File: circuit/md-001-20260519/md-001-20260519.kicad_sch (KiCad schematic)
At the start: 11 parts, among them J1 VIN-motor

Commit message: Update MD基板を更新
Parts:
- added C10, C6, C9: 22n, symbol Device:C_Small
- added C11, C12, C8: 220n, symbol Device:C_Small
- added C4: 100n, symbol Device:C_Small
- added R10, R2, R9: 2.49k, symbol Device:R_Small
- added R11, R13, R5: 10k, symbol Device:R_Small
- added R12, R14, R6: NP, symbol Device:R_Small
- added R15, R16, R8: 20k, symbol Device:R_Small
- added U2, U3, U4: (no value), symbol @Thrive_symbol_md:DRV8874
- renumbered C3 to C1, C4 to C2, C5 to C3, C1 to C5, C2 to C7, R2 to R3, R3 to R4, R4 to R7
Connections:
- net +3.3V: now also C4.1, R11.1, R13.1, R5.1, U2.3 (SLEEP), U3.3 (SLEEP), U4.3 (SLEEP)
- net GND: now also C4.2, R10.2, R12.2, R14.2, R15.2, R16.2, R2.2, R6.2, R8.2, R9.2, U2.15 (GND), U2.16 (PMODE), U2.17 (GND), U2.9 (PGND), U3.15 (GND), U3.16 (PMODE), U3.17 (GND), U3.9 (PGND), U4.15 (GND), U4.16 (PMODE), U4.17 (GND), U4.9 (PGND)
- net VCC: now also C11.2, C12.2, C8.2, U2.11 (VM), U3.11 (VM), U4.11 (VM)
- new net: C12.1, U4.12 (VCP)
- new net: C10.2, U4.13 (CPH)
- new net: C10.1, U4.14 (CPL)
- new net: R10.1, U4.6 (IPROPI)
- new net: C11.1, U3.12 (VCP)
- new net: C9.2, U3.13 (CPH)
- new net: C9.1, U3.14 (CPL)
- new net: R9.1, U3.6 (IPROPI)
- new net: C8.1, U2.12 (VCP)
- new net: C6.2, U2.13 (CPH)
- new net: C6.1, U2.14 (CPL)
- new net: R2.1, U2.6 (IPROPI)
- new net EN-2: U3.1 (EN)
- new net EN-3: U2.1 (EN)
- new net EN-4: U4.1 (EN)
- new net IMODE-2: R15.1, U3.7 (IMODE)
- new net IMODE-3: R8.1, U2.7 (IMODE)
- new net IMODE-4: R16.1, U4.7 (IMODE)
- new net OUT1-2: U3.8 (OUT1)
- new net OUT1-3: U2.8 (OUT1)
- new net OUT1-4: U4.8 (OUT1)
- new net OUT2-2: U3.10 (OUT2)
- new net OUT2-3: U2.10 (OUT2)
- new net OUT2-4: U4.10 (OUT2)
- new net PH-2: U3.2 (PH)
- new net PH-3: U2.2 (PH)
- new net PH-4: U4.2 (PH)
- new net VREF-2: R11.2, R12.1, U3.5 (VREF)
- new net VREF-3: R5.2, R6.1, U2.5 (VREF)
- new net VREF-4: R13.2, R14.1, U4.5 (VREF)
- no-connect marks 1 -> 4
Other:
- moved on the sheet: C1, C2, C3, C5, C7, J1, R1, R3, R4, R7, U1

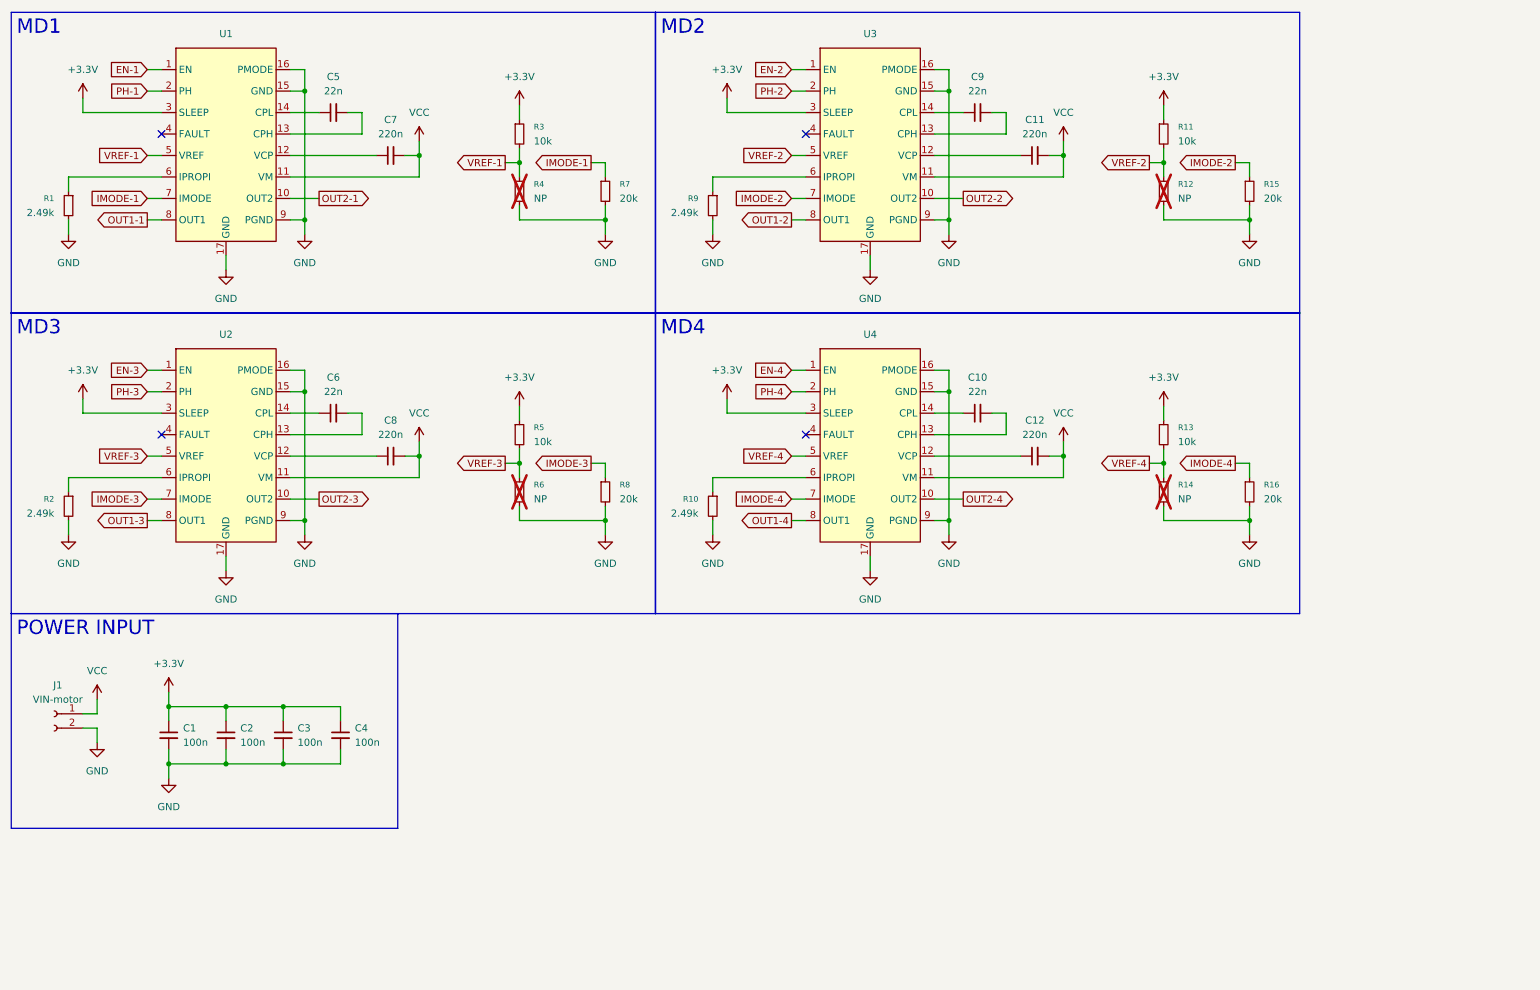
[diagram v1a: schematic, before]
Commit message: Update MD基板の回路図を完成させた
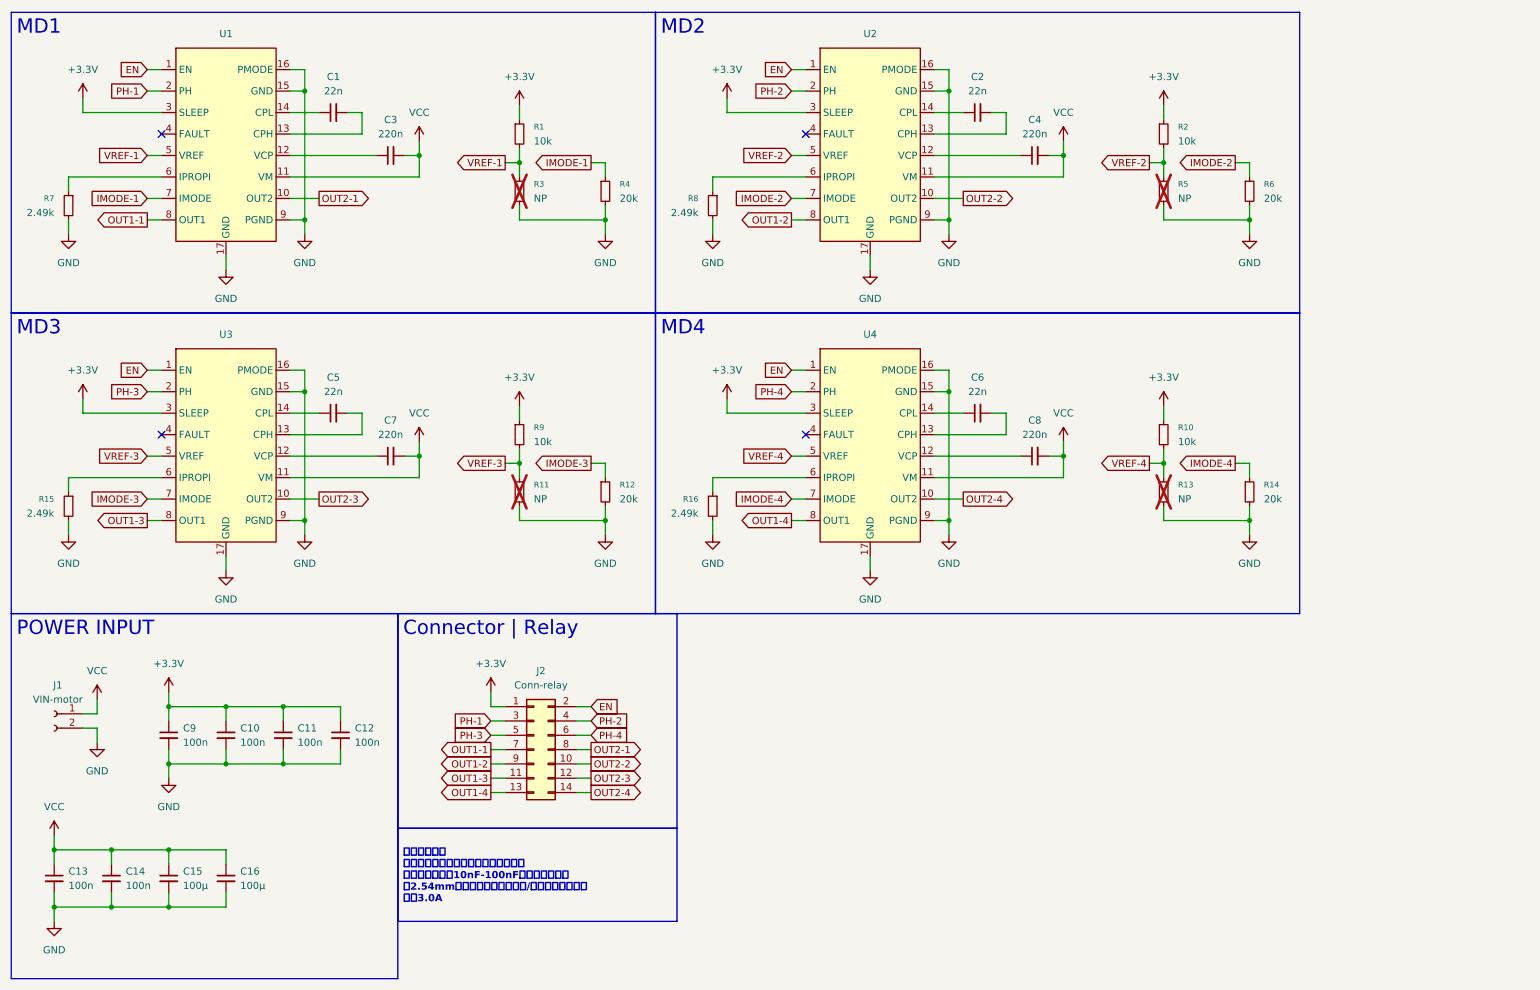
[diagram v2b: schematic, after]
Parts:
- added C13, C14: 100n, Resistor_SMD:R_0603_1608Metric, symbol Device:C_Small
- added C15, C16: 100μ, Resistor_SMD:R_1206_3216Metric, symbol Device:C_Small
- added J2: Conn-relay, Connector_PinSocket_2.54mm:PinSocket_2x07_P2.54mm_Horizontal, symbol Connector_Generic:Conn_02x07_Odd_Even
- C1: renamed from C5; footprint (none) -> Resistor_SMD:R_0603_1608Metric
- C10: renamed from C2; footprint (none) -> Resistor_SMD:R_0603_1608Metric
- C11: renamed from C3; footprint (none) -> Resistor_SMD:R_0603_1608Metric
- C12: renamed from C4; footprint (none) -> Resistor_SMD:R_0603_1608Metric
- C2: renamed from C9; footprint (none) -> Resistor_SMD:R_0603_1608Metric
- C3: renamed from C7; footprint (none) -> Resistor_SMD:R_0603_1608Metric
- C4: renamed from C11; footprint (none) -> Resistor_SMD:R_0603_1608Metric
- C5: renamed from C6; footprint (none) -> Resistor_SMD:R_0603_1608Metric
- C6: renamed from C10; footprint (none) -> Resistor_SMD:R_0603_1608Metric
- C7: renamed from C8; footprint (none) -> Resistor_SMD:R_0603_1608Metric
- C8: renamed from C12; footprint (none) -> Resistor_SMD:R_0603_1608Metric
- C9: renamed from C1; footprint (none) -> Resistor_SMD:R_0603_1608Metric
- J1: footprint (none) -> Connector_AMASS:AMASS_XT30PW-F_1x02_P2.50mm_Horizontal
- R1: renamed from R3; footprint (none) -> Resistor_SMD:R_0603_1608Metric
- R10: renamed from R13; footprint (none) -> Resistor_SMD:R_0603_1608Metric
- R11: renamed from R6; footprint (none) -> Resistor_SMD:R_0603_1608Metric
- R12: renamed from R8; footprint (none) -> Resistor_SMD:R_0603_1608Metric
- R13: renamed from R14; footprint (none) -> Resistor_SMD:R_0603_1608Metric
- R14: renamed from R16; footprint (none) -> Resistor_SMD:R_0603_1608Metric
- R15: renamed from R2; footprint (none) -> Resistor_SMD:R_0603_1608Metric
- R16: renamed from R10; footprint (none) -> Resistor_SMD:R_0603_1608Metric
- R2: renamed from R11; footprint (none) -> Resistor_SMD:R_0603_1608Metric
- R3: renamed from R4; footprint (none) -> Resistor_SMD:R_0603_1608Metric
- R4: renamed from R7; footprint (none) -> Resistor_SMD:R_0603_1608Metric
- R5: renamed from R12; footprint (none) -> Resistor_SMD:R_0603_1608Metric
- R6: renamed from R15; footprint (none) -> Resistor_SMD:R_0603_1608Metric
- R7: renamed from R1; footprint (none) -> Resistor_SMD:R_0603_1608Metric
- R8: renamed from R9; footprint (none) -> Resistor_SMD:R_0603_1608Metric
- R9: renamed from R5; footprint (none) -> Resistor_SMD:R_0603_1608Metric
- U1, U4: footprint (none) -> Package_SO:HTSSOP-16-1EP_4.4x5mm_P0.65mm_EP3.4x5mm_Mask2.66x2.46mm
- U2: renamed from U3; footprint (none) -> Package_SO:HTSSOP-16-1EP_4.4x5mm_P0.65mm_EP3.4x5mm_Mask2.66x2.46mm
- U3: renamed from U2; footprint (none) -> Package_SO:HTSSOP-16-1EP_4.4x5mm_P0.65mm_EP3.4x5mm_Mask2.66x2.46mm
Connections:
- net EN-2 is gone; now on net EN: U2.1 (EN)
- net EN-3 is gone; now on net EN: U3.1 (EN)
- net EN-4 is gone; now on net EN: U4.1 (EN)
- net +3.3V: now also J2.1 (Pin_1)
- net GND: now also C13.2, C14.2, C15.2, C16.2
- net OUT1-1: now also J2.7 (Pin_7)
- net OUT1-2: now also J2.9 (Pin_9)
- net OUT1-3: now also J2.11 (Pin_11)
- net OUT1-4: now also J2.13 (Pin_13)
- net OUT2-1: now also J2.8 (Pin_8)
- net OUT2-2: now also J2.10 (Pin_10)
- net OUT2-3: now also J2.12 (Pin_12)
- net OUT2-4: now also J2.14 (Pin_14)
- net PH-1: now also J2.3 (Pin_3)
- net PH-2: now also J2.4 (Pin_4)
- net PH-3: now also J2.5 (Pin_5)
- net PH-4: now also J2.6 (Pin_6)
- net VCC: now also C13.1, C14.1, C15.1, C16.1
- net EN-1 renamed EN
- net EN: now also J2.2 (Pin_2)

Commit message: Update いったんMD完成
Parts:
- removed C14: 100n, Resistor_SMD:R_0603_1608Metric, symbol Device:C_Small
- removed C16: 100μ, Resistor_SMD:R_1206_3216Metric, symbol Device:C_Small
- renumbered C15 to C14
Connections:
- net +3.3V: now also J2.4 (Pin_4); no longer J2.1 (Pin_1)
- net EN: now also J2.6 (Pin_6); no longer J2.2 (Pin_2)
- net OUT1-1: now also J2.2 (Pin_2); no longer J2.7 (Pin_7)
- net OUT1-2: now also J2.3 (Pin_3); no longer J2.9 (Pin_9)
- net OUT1-3: now also J2.7 (Pin_7); no longer J2.11 (Pin_11)
- net OUT1-4: now also J2.11 (Pin_11); no longer J2.13 (Pin_13)
- net OUT2-1: now also J2.1 (Pin_1); no longer J2.8 (Pin_8)
- net OUT2-2: now also J2.5 (Pin_5); no longer J2.10 (Pin_10)
- net OUT2-3: now also J2.9 (Pin_9); no longer J2.12 (Pin_12)
- net OUT2-4: now also J2.13 (Pin_13); no longer J2.14 (Pin_14)
- net PH-1: now also J2.8 (Pin_8); no longer J2.3 (Pin_3)
- net PH-2: now also J2.10 (Pin_10); no longer J2.4 (Pin_4)
- net PH-3: now also J2.12 (Pin_12); no longer J2.5 (Pin_5)
- net PH-4: now also J2.14 (Pin_14); no longer J2.6 (Pin_6)
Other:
- moved on the sheet: C14

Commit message: Update DRしてもらったのでMDを修正更新
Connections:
- net GND: now also J1.1 (Pin_1); no longer J1.2 (Pin_2)
- net VCC: now also J1.2 (Pin_2); no longer J1.1 (Pin_1)
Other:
- moved on the sheet: J1
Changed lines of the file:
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@@
 	(symbol
 		(lib_id "Connector:Conn_01x02_Socket")
-		(at 20.32 137.16 0)
-		(mirror y)
+		(at 20.32 139.7 180)
 		(unit 1)
 		(body_style 1)
@@
 		(in_pos_files yes)
 		(dnp no)
-		(fields_autoplaced yes)
 		(property "Reference" "J1"
-			(at 20.955 132.08 0)
+			(at 20.955 144.78 0)
 			(show_name no)
 			(do_not_autoplace no)
@@
 		)
 		(property "Value" "VIN-motor"
-			(at 20.955 134.62 0)
+			(at 20.955 142.24 0)
 			(show_name no)
 			(do_not_autoplace no)
@@
 		)
 		(property "Footprint" "Connector_AMASS:AMASS_XT30PW-F_1x02_P2.50mm_Horizontal"
-			(at 20.32 137.16 0)
+			(at 20.32 139.7 0)
 			(hide yes)
 			(show_name no)
@@
 		)
 		(property "Datasheet" ""
-			(at 20.32 137.16 0)
+			(at 20.32 139.7 0)
 			(hide yes)
 			(show_name no)
@@
 		)
 		(property "Description" "Generic connector, single row, 01x02, script generated"
-			(at 20.32 137.16 0)
+			(at 20.32 139.7 0)
 			(hide yes)
 			(show_name no)

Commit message: Update MD基板を更新
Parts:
- removed J2: Conn-relay, Connector_PinSocket_2.54mm:PinSocket_2x07_P2.54mm_Horizontal, symbol Connector_Generic:Conn_02x07_Odd_Even
- added J2: Conn_Ball_Catch, Connector_PinSocket_2.54mm:PinSocket_1x03_P2.54mm_Vertical, symbol Connector:Conn_01x03_Socket
- added J3: Conn_relay, Connector_PinSocket_2.54mm:PinSocket_2x08_P2.54mm_Horizontal, symbol Connector_Generic:Conn_02x08_Odd_Even
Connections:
- net +3.3V: now also J2.2 (Pin_2), J3.2 (Pin_2)
- net EN: now also J3.6 (Pin_6)
- net GND: now also J2.3 (Pin_3), J3.4 (Pin_4)
- net OUT1-1: now also J3.1 (Pin_1)
- net OUT1-2: now also J3.5 (Pin_5)
- net OUT1-3: now also J3.9 (Pin_9)
- net OUT1-4: now also J3.13 (Pin_13)
- net OUT2-1: now also J3.3 (Pin_3)
- net OUT2-2: now also J3.7 (Pin_7)
- net OUT2-3: now also J3.11 (Pin_11)
- net OUT2-4: now also J3.15 (Pin_15)
- net PH-1: now also J3.8 (Pin_8)
- net PH-2: now also J3.10 (Pin_10)
- net PH-3: now also J3.12 (Pin_12)
- net PH-4: now also J3.14 (Pin_14)
- new net BALL_CATCH: J2.1 (Pin_1), J3.16 (Pin_16)

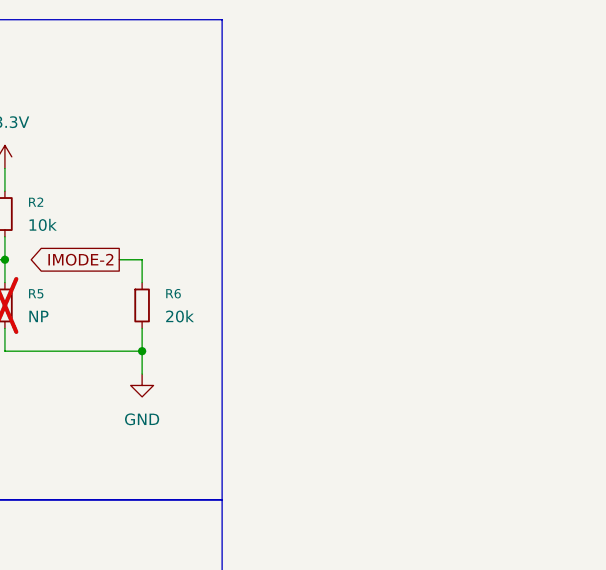
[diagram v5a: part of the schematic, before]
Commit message: Update MD基板のボード図を更新
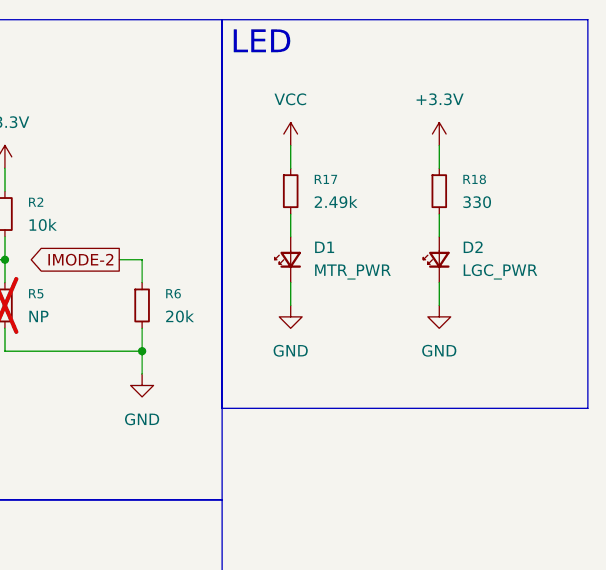
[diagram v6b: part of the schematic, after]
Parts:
- added D1: MTR_PWR, LED_SMD:LED_0603_1608Metric, symbol Device:LED_Small
- added D2: LGC_PWR, LED_SMD:LED_0603_1608Metric, symbol Device:LED_Small
- added R17: 2.49k, Resistor_SMD:R_0603_1608Metric, symbol Device:R_Small
- added R18: 330, Resistor_SMD:R_0603_1608Metric, symbol Device:R_Small
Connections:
- net +3.3V: now also R18.1
- net GND: now also D1.1 (K), D2.1 (K)
- net VCC: now also R17.1
- new net: D1.2 (A), R17.2
- new net: D2.2 (A), R18.2

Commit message: Create 供給基板の回路図完成
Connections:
- net BALL_CATCH renamed BallCatch_{Back}
- net EN renamed Motor_{EN}
- net OUT1-1 renamed Motor_{OUT1-1}
- net OUT1-2 renamed Motor_{OUT2-1}
- net OUT1-3 renamed Motor_{OUT3-1}
- net OUT1-4 renamed Motor_{OUT4-1}
- net OUT2-1 renamed Motor_{OUT1-2}
- net OUT2-2 renamed Motor_{OUT2-2}
- net OUT2-3 renamed Motor_{OUT3-2}
- net OUT2-4 renamed Motor_{OUT4-2}
- net PH-1 renamed Motor1_{PWM}
- net PH-2 renamed Motor2_{PWM}
- net PH-3 renamed Motor3_{PWM}
- net PH-4 renamed Motor4_{PWM}

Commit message: Update MD基板のSMD部品のサイズ変更を完了した
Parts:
- C1, C10, C11, C12, C13, C2, C3, C4, C5, C6, C7, C8, C9, R1, R10, R11, R12, R13, R14, R15, R16, R17, R18, R2, R3, R4, R5, R6, R7, R8, R9: footprint Resistor_SMD:R_0603_1608Metric -> Resistor_SMD:R_0805_2012Metric
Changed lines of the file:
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@@
 			)
 		)
-		(property "Footprint" "Resistor_SMD:R_0603_1608Metric"
+		(property "Footprint" "Resistor_SMD:R_0805_2012Metric"
 			(at 137.16 46.99 0)
 			(hide yes)
@@
 			)
 		)
-		(property "Footprint" "Resistor_SMD:R_0603_1608Metric"
+		(property "Footprint" "Resistor_SMD:R_0805_2012Metric"
 			(at 217.17 44.45 0)
 			(hide yes)
@@
 			)
 		)
-		(property "Footprint" "Resistor_SMD:R_0603_1608Metric"
+		(property "Footprint" "Resistor_SMD:R_0805_2012Metric"
 			(at 102.87 34.29 0)
 			(hide yes)
@@
 			)
 		)
-		(property "Footprint" "Resistor_SMD:R_0603_1608Metric"
+		(property "Footprint" "Resistor_SMD:R_0805_2012Metric"
 			(at 22.86 46.99 0)
 			(hide yes)
@@
 			)
 		)
-		(property "Footprint" "Resistor_SMD:R_0603_1608Metric"
+		(property "Footprint" "Resistor_SMD:R_0805_2012Metric"
 			(at 137.16 100.33 0)
 			(hide yes)
@@
 			)
 		)
-		(property "Footprint" "Resistor_SMD:R_0603_1608Metric"
+		(property "Footprint" "Resistor_SMD:R_0805_2012Metric"
 			(at 248.92 31.75 0)
 			(hide yes)
@@
 			)
 		)
-		(property "Footprint" "Resistor_SMD:R_0603_1608Metric"
+		(property "Footprint" "Resistor_SMD:R_0805_2012Metric"
 			(at 80.01 91.44 0)
 			(hide yes)
@@
 			)
 		)
-		(property "Footprint" "Resistor_SMD:R_0603_1608Metric"
+		(property "Footprint" "Resistor_SMD:R_0805_2012Metric"
 			(at 60.96 140.97 0)
 			(hide yes)
@@
 			)
 		)
-		(property "Footprint" "Resistor_SMD:R_0603_1608Metric"
+		(property "Footprint" "Resistor_SMD:R_0805_2012Metric"
 			(at 217.17 34.29 0)
 			(hide yes)
@@
 			)
 		)
-		(property "Footprint" "Resistor_SMD:R_0603_1608Metric"
+		(property "Footprint" "Resistor_SMD:R_0805_2012Metric"
 			(at 184.15 30.48 0)
 			(hide yes)
@@
 			)
 		)
-		(property "Footprint" "Resistor_SMD:R_0603_1608Metric"
+		(property "Footprint" "Resistor_SMD:R_0805_2012Metric"
 			(at 265.43 31.75 0)
 			(hide yes)
@@
 			)
 		)
-		(property "Footprint" "Resistor_SMD:R_0603_1608Metric"
+		(property "Footprint" "Resistor_SMD:R_0805_2012Metric"
 			(at 118.11 44.45 0)
 			(hide yes)
@@
 			)
 		)
-		(property "Footprint" "Resistor_SMD:R_0603_1608Metric"
+		(property "Footprint" "Resistor_SMD:R_0805_2012Metric"
 			(at 217.17 87.63 0)
 			(hide yes)
@@
 			)
 		)
-		(property "Footprint" "Resistor_SMD:R_0603_1608Metric"
+		(property "Footprint" "Resistor_SMD:R_0805_2012Metric"
 			(at 50.8 140.97 0)
 			(hide yes)
@@
 			)
 		)
-		(property "Footprint" "Resistor_SMD:R_0603_1608Metric"
+		(property "Footprint" "Resistor_SMD:R_0805_2012Metric"
 			(at 22.86 100.33 0)
 			(hide yes)
@@
 			)
 		)
-		(property "Footprint" "Resistor_SMD:R_0603_1608Metric"
+		(property "Footprint" "Resistor_SMD:R_0805_2012Metric"
 			(at 20.32 166.37 0)
 			(hide yes)
@@
 			)
 		)
-		(property "Footprint" "Resistor_SMD:R_0603_1608Metric"
+		(property "Footprint" "Resistor_SMD:R_0805_2012Metric"
 			(at 69.85 83.82 0)
 			(hide yes)
@@
 			)
 		)
-		(property "Footprint" "Resistor_SMD:R_0603_1608Metric"
+		(property "Footprint" "Resistor_SMD:R_0805_2012Metric"
 			(at 71.12 140.97 0)
 			(hide yes)
@@
 			)
 		)
-		(property "Footprint" "Resistor_SMD:R_0603_1608Metric"
+		(property "Footprint" "Resistor_SMD:R_0805_2012Metric"
 			(at 102.87 44.45 0)
 			(hide yes)
@@
 			)
 		)
-		(property "Footprint" "Resistor_SMD:R_0603_1608Metric"
+		(property "Footprint" "Resistor_SMD:R_0805_2012Metric"
 			(at 69.85 30.48 0)
 			(hide yes)
@@
 			)
 		)
-		(property "Footprint" "Resistor_SMD:R_0603_1608Metric"
+		(property "Footprint" "Resistor_SMD:R_0805_2012Metric"
 			(at 232.41 44.45 0)
 			(hide yes)
@@
 			)
 		)
-		(property "Footprint" "Resistor_SMD:R_0603_1608Metric"
+		(property "Footprint" "Resistor_SMD:R_0805_2012Metric"
 			(at 118.11 97.79 0)
 			(hide yes)
@@
 			)
 		)
-		(property "Footprint" "Resistor_SMD:R_0603_1608Metric"
+		(property "Footprint" "Resistor_SMD:R_0805_2012Metric"
 			(at 184.15 83.82 0)
 			(hide yes)
@@
 			)
 		)
-		(property "Footprint" "Resistor_SMD:R_0603_1608Metric"
+		(property "Footprint" "Resistor_SMD:R_0805_2012Metric"
 			(at 102.87 87.63 0)
 			(hide yes)
@@
 			)
 		)
-		(property "Footprint" "Resistor_SMD:R_0603_1608Metric"
+		(property "Footprint" "Resistor_SMD:R_0805_2012Metric"
 			(at 194.31 91.44 0)
 			(hide yes)
@@
 			)
 		)
-		(property "Footprint" "Resistor_SMD:R_0603_1608Metric"
+		(property "Footprint" "Resistor_SMD:R_0805_2012Metric"
 			(at 80.01 38.1 0)
 			(hide yes)
@@
 			)
 		)
-		(property "Footprint" "Resistor_SMD:R_0603_1608Metric"
+		(property "Footprint" "Resistor_SMD:R_0805_2012Metric"
 			(at 40.64 140.97 0)
 			(hide yes)
@@
 			)
 		)
-		(property "Footprint" "Resistor_SMD:R_0603_1608Metric"
+		(property "Footprint" "Resistor_SMD:R_0805_2012Metric"
 			(at 102.87 97.79 0)
 			(hide yes)
@@
 			)
 		)
-		(property "Footprint" "Resistor_SMD:R_0603_1608Metric"
+		(property "Footprint" "Resistor_SMD:R_0805_2012Metric"
 			(at 232.41 97.79 0)
 			(hide yes)
@@
 			)
 		)
-		(property "Footprint" "Resistor_SMD:R_0603_1608Metric"
+		(property "Footprint" "Resistor_SMD:R_0805_2012Metric"
 			(at 217.17 97.79 0)
 			(hide yes)
@@
 			)
 		)
-		(property "Footprint" "Resistor_SMD:R_0603_1608Metric"
+		(property "Footprint" "Resistor_SMD:R_0805_2012Metric"
 			(at 194.31 38.1 0)
 			(hide yes)
